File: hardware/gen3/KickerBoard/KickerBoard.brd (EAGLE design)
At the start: 130 x 100 mm, 107 parts, among them Q6 MOSFET-PCHANNEL, U1 NC7WZ08K8X, U2 ATMEGA165PV-8AU

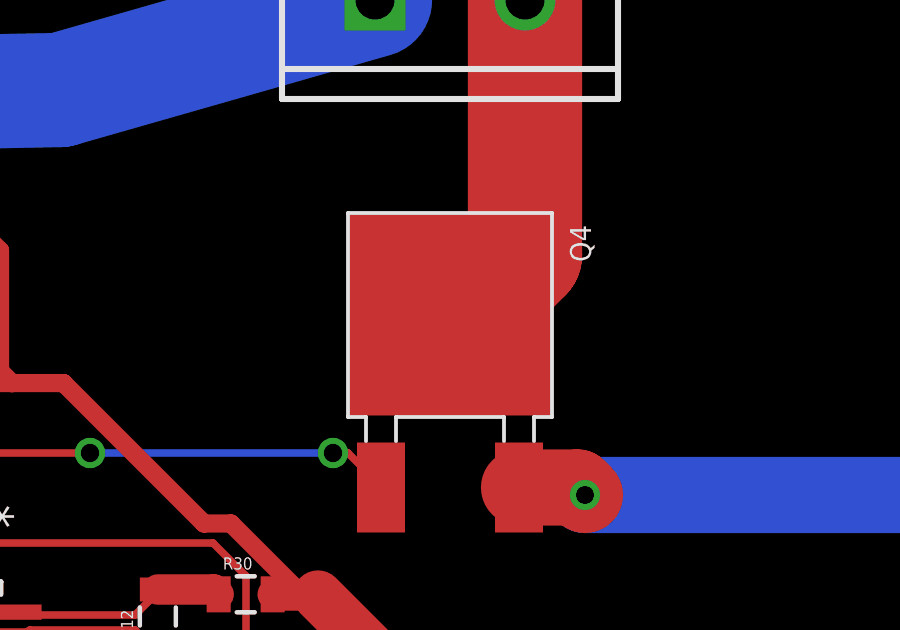
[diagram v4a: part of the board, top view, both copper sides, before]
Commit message: wider traces for gates
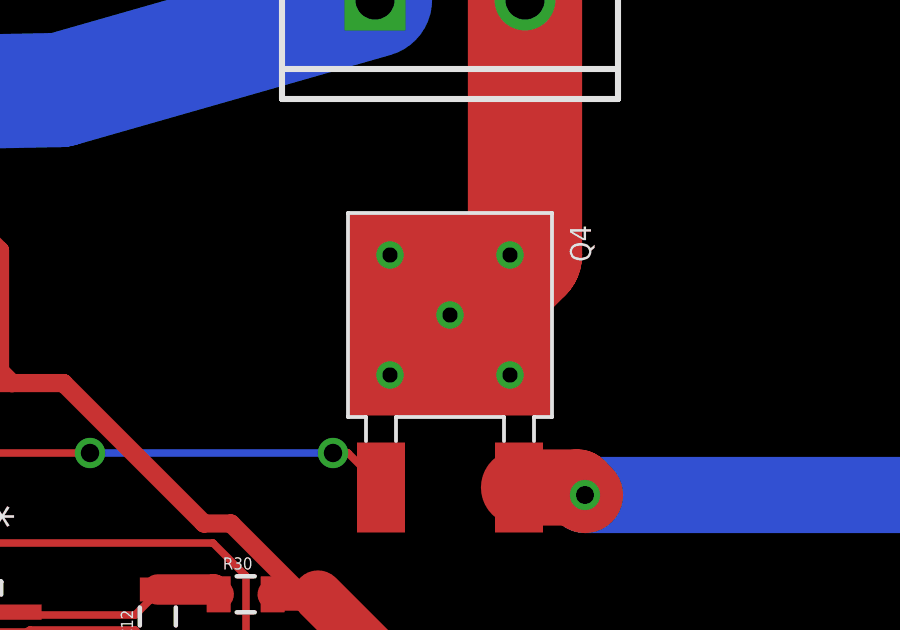
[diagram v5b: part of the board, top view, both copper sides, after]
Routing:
- net N$15: vias 0 -> 1
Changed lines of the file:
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@@
 <wire x1="-104" y1="2.69" x2="-110.1" y2="2" width="0" layer="19" extent="1-1"/>
 <wire x1="3.3" y1="7.7" x2="-104" y2="2.69" width="0" layer="19" extent="1-1"/>
-<wire x1="21" y1="22.6" x2="21" y2="20.5" width="0" layer="19" extent="1-1"/>
 </signal>
 <signal name="3.3V">
@@
 <wire x1="54.75" y1="84.75" x2="54" y2="84" width="3.81" layer="1"/>
 <wire x1="54.5" y1="85" x2="54.75" y2="84.75" width="0.254" layer="1"/>
+<via x="54.5" y="85" extent="1-16" drill="0.508"/>
 </signal>
 <signal name="5V">
@@
 <wire x1="63.2499" y1="70.5501" x2="63.2499" y2="68.9" width="0.4064" layer="1"/>
 </signal>
+<signal name="N$37">
+<via x="52.5" y="87" extent="1-16" drill="0.508"/>
+</signal>
+<signal name="N$38">
+<via x="52.5" y="83" extent="1-16" drill="0.508"/>
+</signal>
+<signal name="N$44">
+<via x="56.5" y="87" extent="1-16" drill="0.508"/>
+</signal>
+<signal name="N$45">
+<via x="56.5" y="83" extent="1-16" drill="0.508"/>
+</signal>
 </signals>

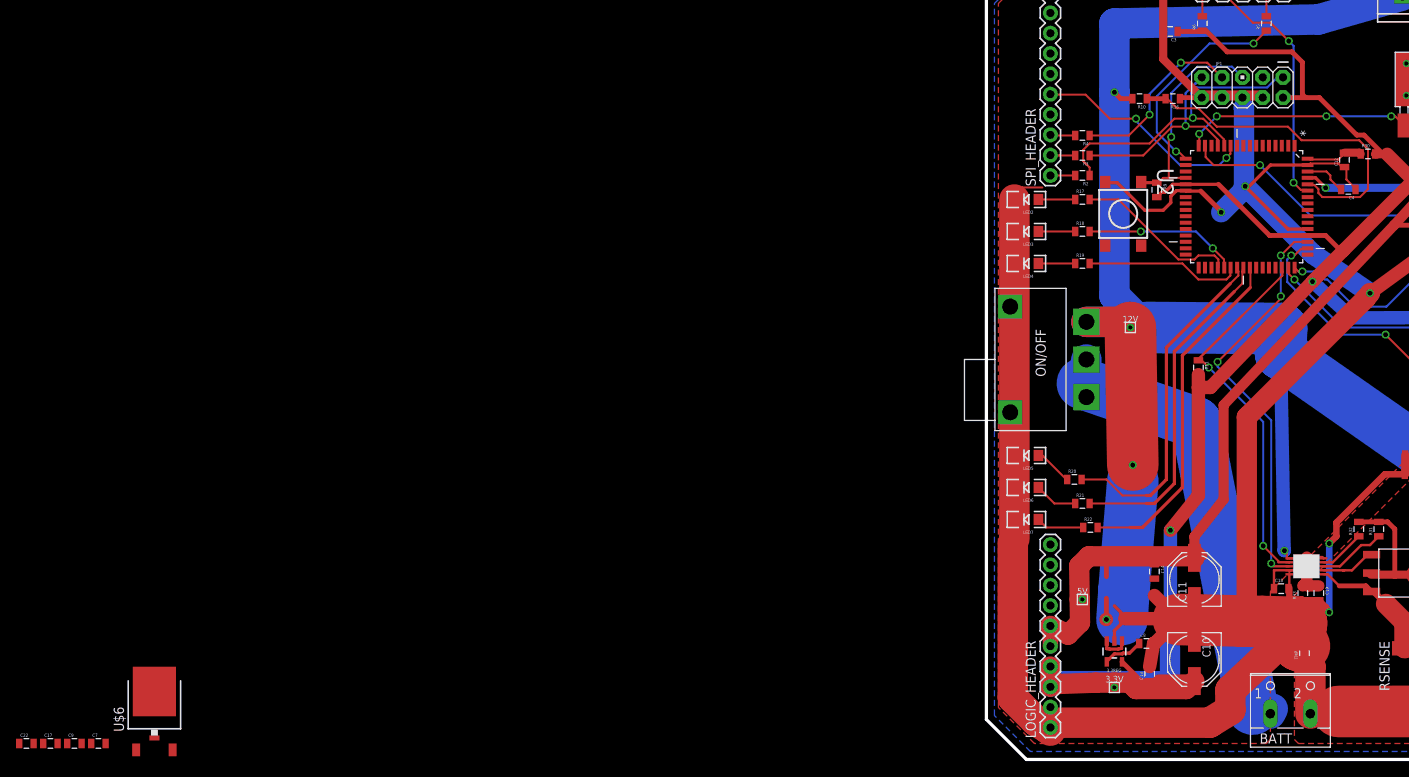
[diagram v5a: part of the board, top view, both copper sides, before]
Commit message: finished motor. kicker still needs work
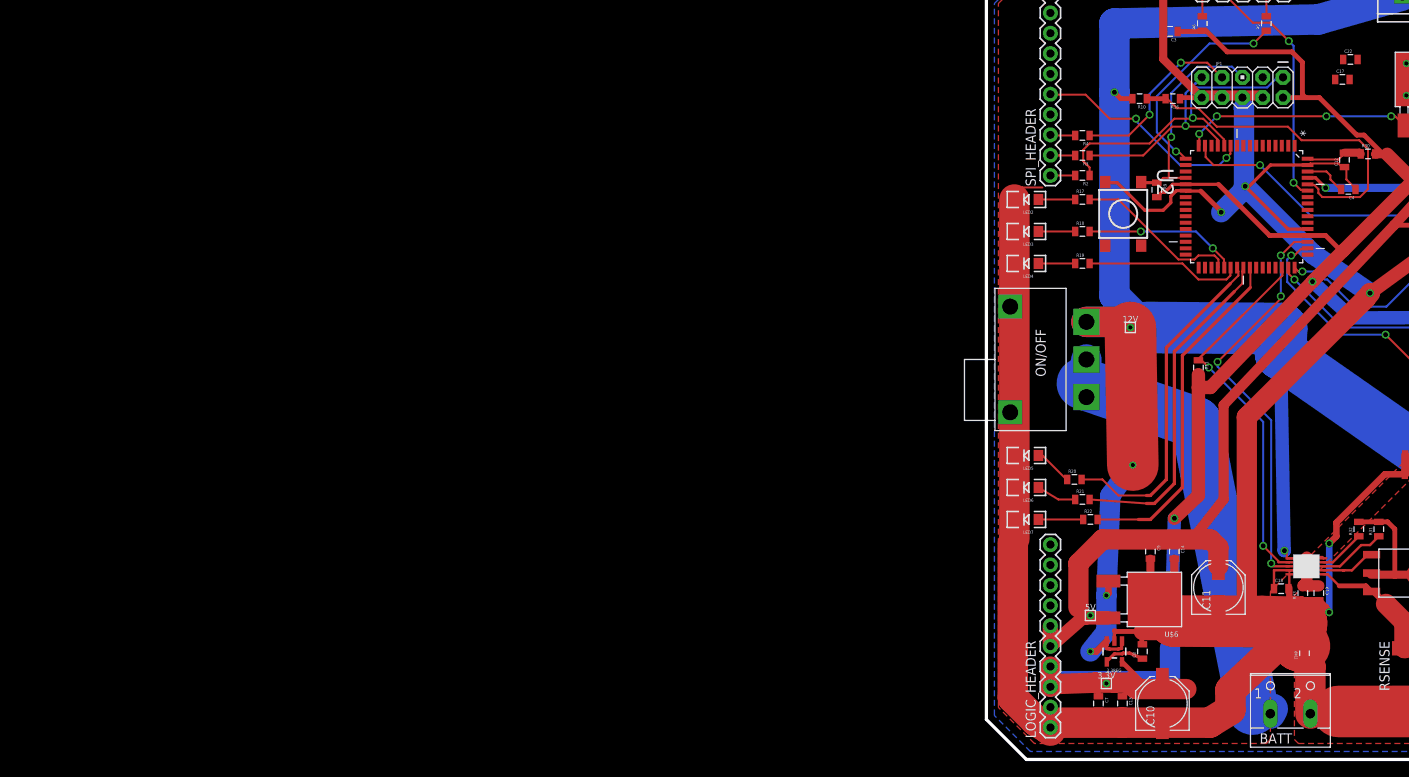
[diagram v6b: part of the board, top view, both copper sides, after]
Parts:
- U$6: value 3.3REG1A -> 3.3REG1AREG; device gen3:3.3REG1A -> gen3:DPAK
- moved C22 186.3 mm to (45.5, 87.5)
- moved C17 181.6 mm to (44.5, 85.0)
- moved C9 136.6 mm to (20.5, 26.0), turned to 270 degrees
- moved U$6 125.8 mm to (21.0, 20.0), turned to 180 degrees
- moved C7 125.1 mm to (14.0, 7.00), turned to 270 degrees
- moved C10 6.80 mm to (22.0, 7.00), turned to 90 degrees
- moved C13 5.02 mm to (17.0, 7.00), turned to 270 degrees
- moved C14 3.54 mm to (23.5, 26.0)
- moved C11 3.16 mm to (29.0, 21.5)
- moved 5V 2.24 mm to (13.0, 18.0)
- moved 3.3V 1.12 mm to (15.0, 9.50)
- moved C8 1.12 mm to (19.5, 13.5), turned to 90 degrees
- moved R22 1.00 mm to (13.0, 30.0)
- moved R21 0.50 mm to (12.0, 32.5)
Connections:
- net 12V: now also U$6.GATE; no longer U$6.FIN, U$6.IN
- net 5V: now also U$6.SOURCE; no longer U$6.OUT
- net GND: now also U$6.DRAIN; no longer U$6.NC
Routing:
- net GND: track 493.5 -> 509.2 mm
- net 12V: track 394.2 -> 399.6 mm, vias 8 -> 9
- net 5V: track 124.4 -> 127.6 mm
- net 3.3V: track 251.1 -> 253.5 mm

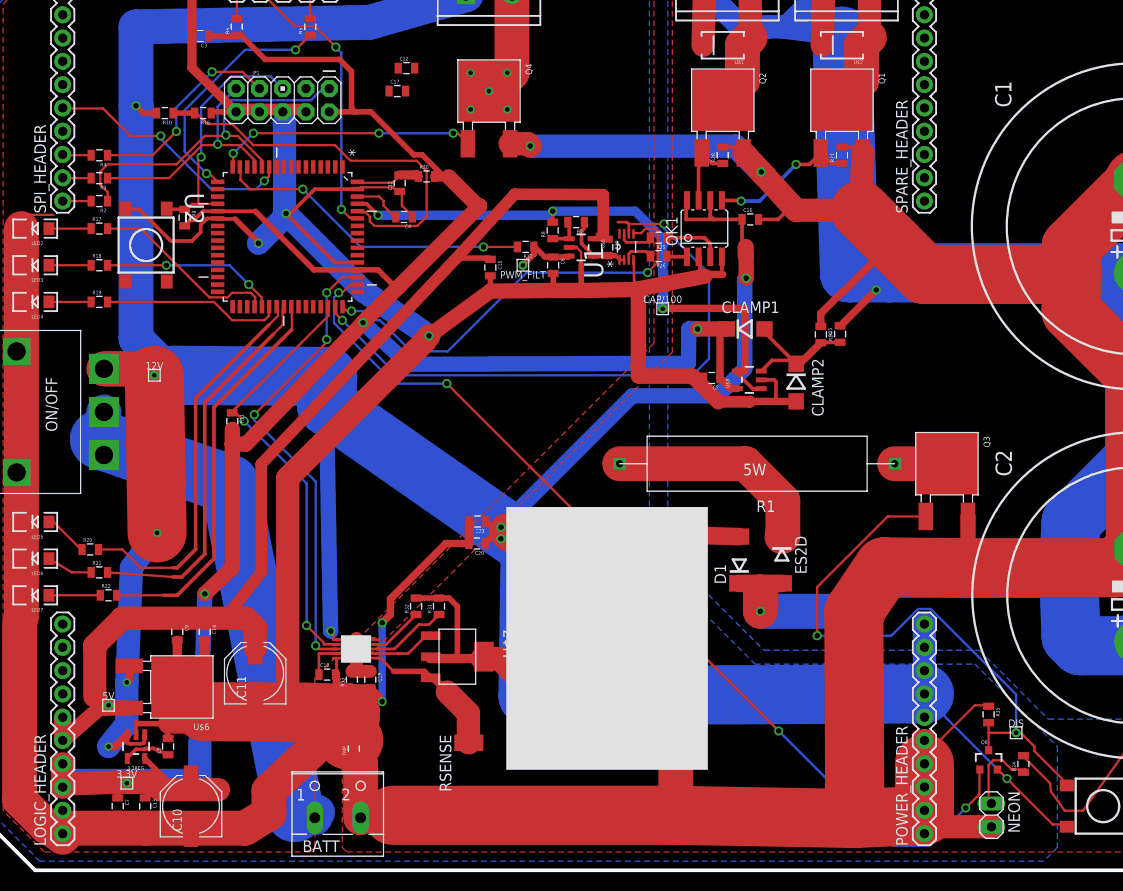
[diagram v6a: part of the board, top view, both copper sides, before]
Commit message: finalized kicker board
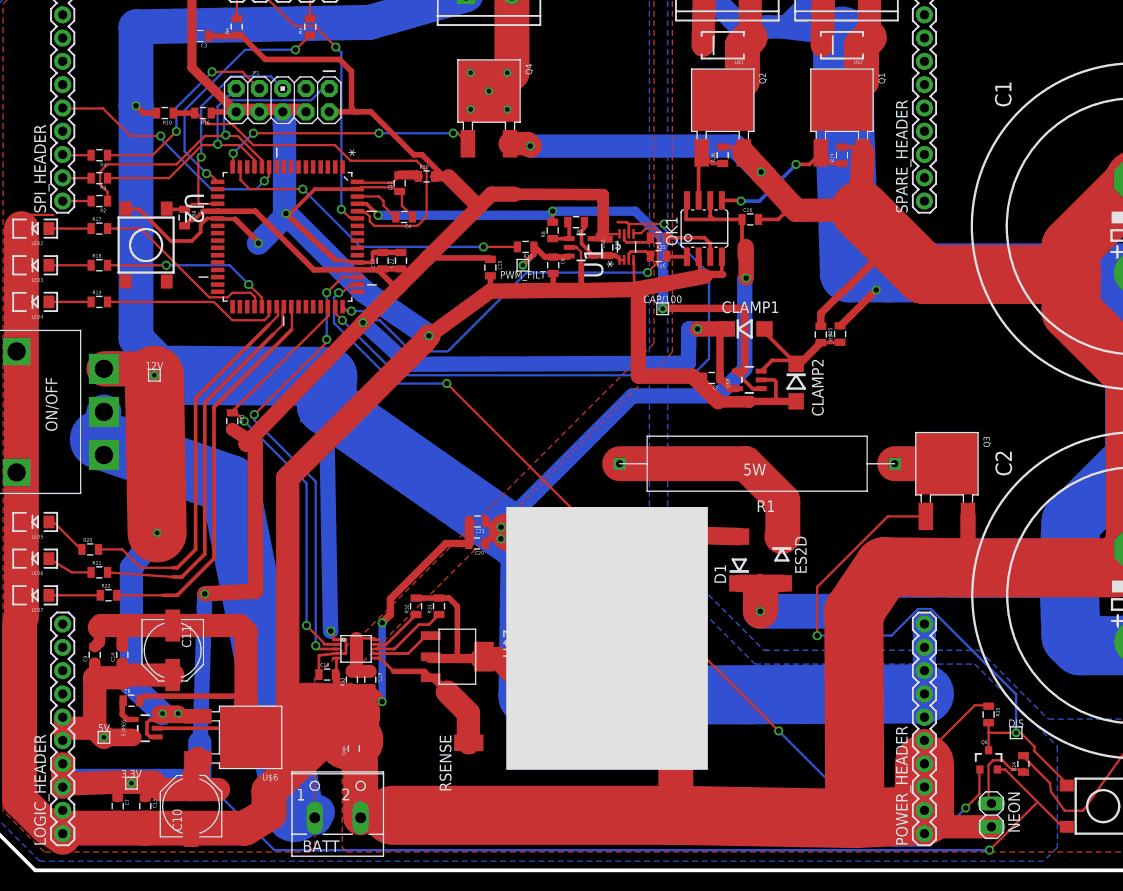
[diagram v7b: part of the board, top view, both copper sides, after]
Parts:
- removed 3.3REG: (no value), SparkFun-PowerIC:SOT23-5
- added 5.0REG: MIC5219 5V, SparkFun-PowerIC:SOT23-5
- moved C22 21.0 mm to (44.9, 66.5), turned to 90 degrees
- moved C17 18.6 mm to (42.9, 66.5), turned to 90 degrees
- moved C11 9.34 mm to (20.0, 24.0), turned to 270 degrees
- moved C14 9.34 mm to (14.5, 23.5), turned to 90 degrees
- moved C9 9.34 mm to (11.5, 23.5), turned to 90 degrees
- moved U$6 9.30 mm to (28.5, 14.5)
- moved C8 6.40 mm to (15.5, 18.5), turned to 0 degrees
- moved 5V 3.54 mm to (12.5, 14.5)
- moved 3.3V 0.50 mm to (15.5, 9.50)
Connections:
- removed net N$18: 3.3REG.4, C8.1
- new net N$16: 5.0REG.4, C8.1
- net 12V: now also 5.0REG.1, 5.0REG.3; no longer 3.3REG.1, 3.3REG.3
- net 3.3V: now also U$6.SOURCE; no longer 3.3REG.5
- net 5V: now also 5.0REG.5; no longer U$6.SOURCE
- net GND: now also 5.0REG.2; no longer 3.3REG.2
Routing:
- net 3.3V: track 253.5 -> 395.8 mm, vias 3 -> 4
- net 5V: track 127.6 -> 28.8 mm
- net GND: track 509.2 -> 535.7 mm
- net 12V: track 399.6 -> 378.6 mm, vias 9 -> 8
- net N$15: track 13.1 -> 20.8 mm, vias 1 -> 5
- net N$18: track 5.08 -> 0.00 mm
- net N$16: track 0.00 -> 2.97 mm

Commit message: added logos. generated gerbers
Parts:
- added U$9: LOGO, gen3:LOGO
- moved U$6 0.50 mm to (28.5, 15.0)
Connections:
- net N$19: now also ON/OFF.IN1
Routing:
- net N$19: track 57.7 -> 59.6 mm
- net 3.3V: track 395.8 -> 396.3 mm
